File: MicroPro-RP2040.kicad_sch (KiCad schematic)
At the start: 55 parts, among them J1 USB_C_Receptacle_USB2.0_16P, J2 Qwiic, J3 Conn_02x12_Counter_Clockwise, J4 Conn_01x04, SW1 Boot, SW2 Reset, U1 RP2040, U2 AP2112K-3.3, U3 W25Q128JV, U5 TMUX1204DQAR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

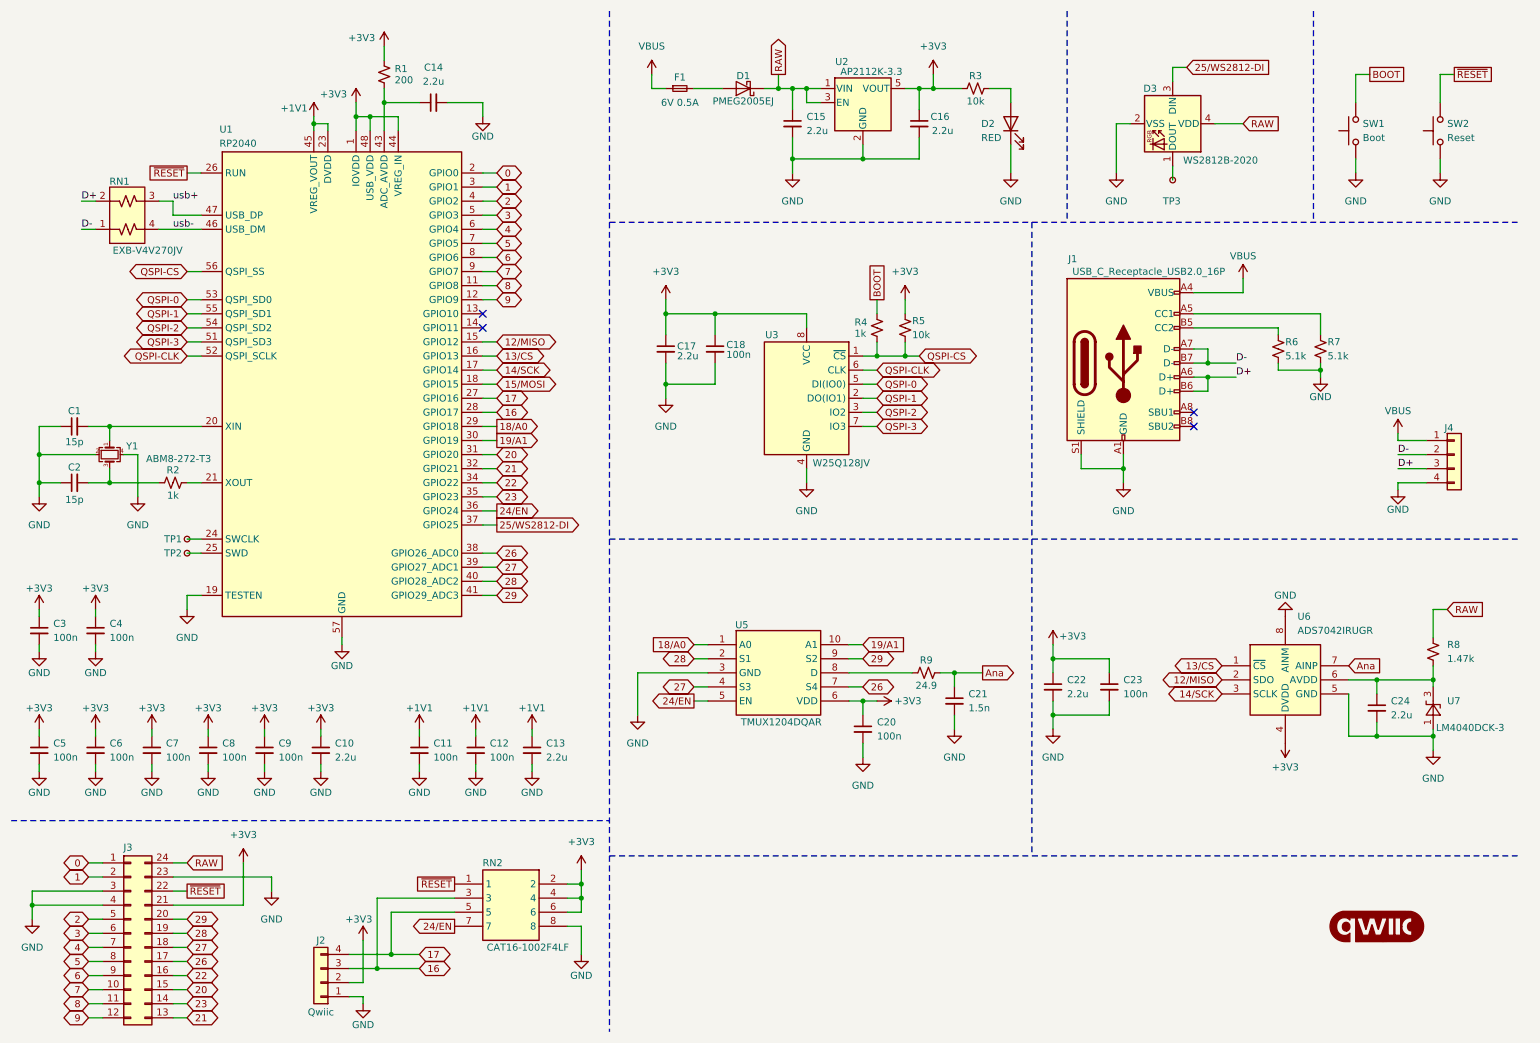
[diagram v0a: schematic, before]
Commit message: fixed miswiring in schematics, v1.1 board
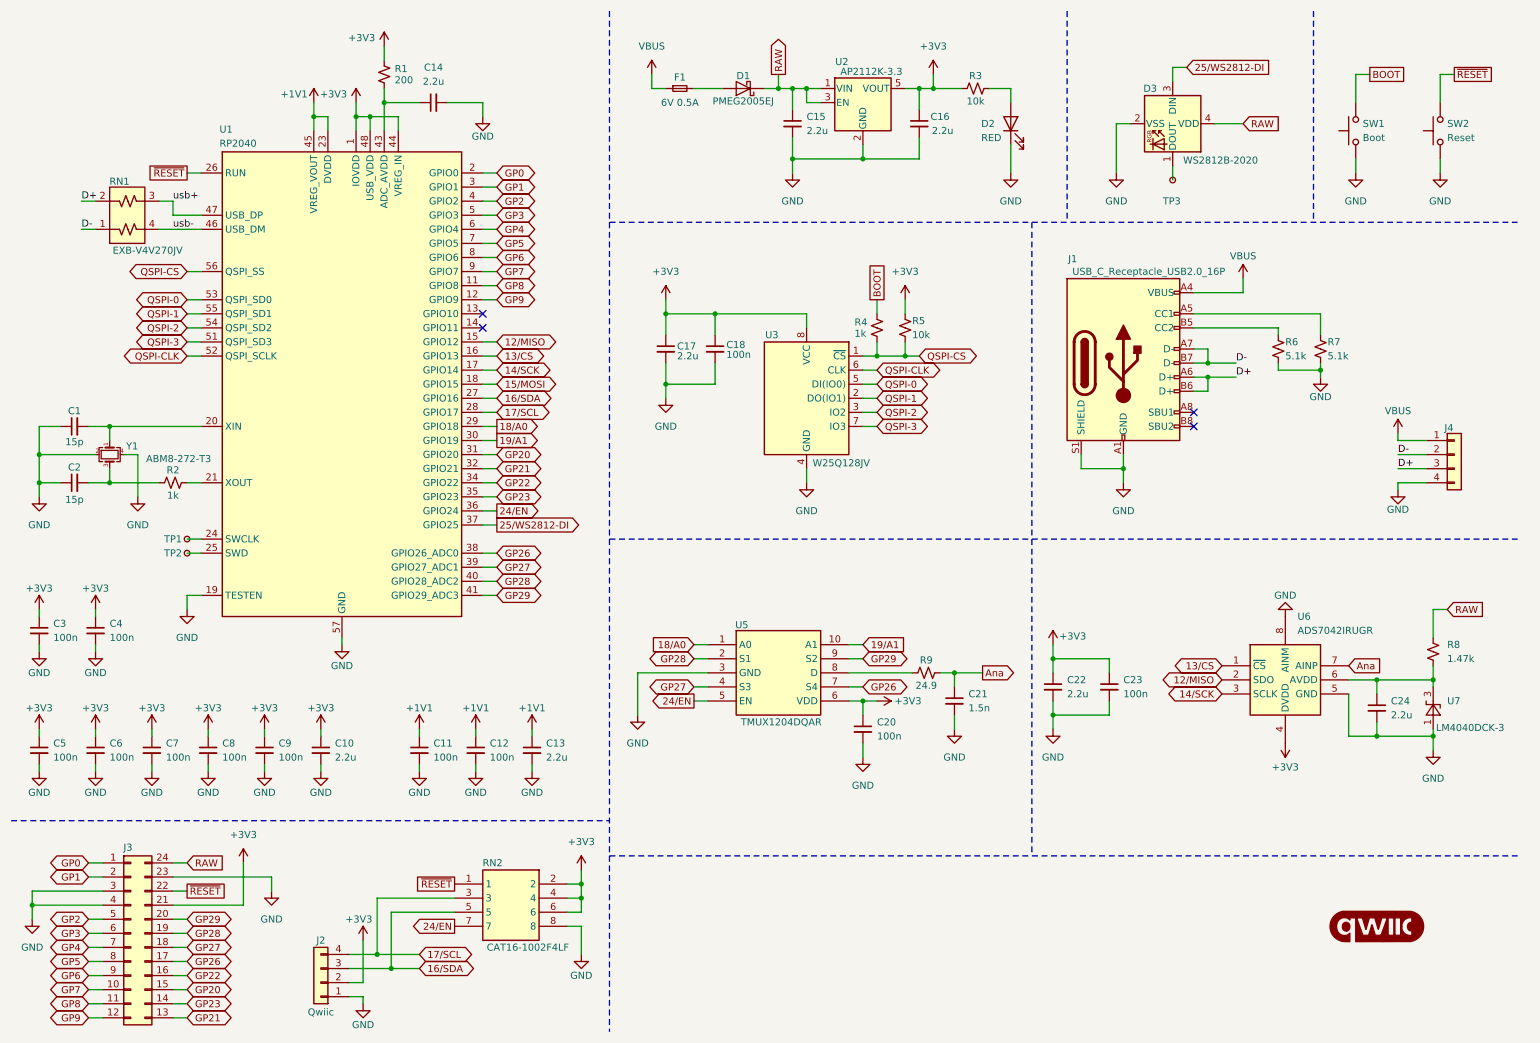
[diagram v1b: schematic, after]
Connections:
- net 0 renamed GP0
- net 1 renamed GP1
- net 16 renamed 17/SCL
- net 17/SCL: now also J2.4 (Pin_4); no longer J2.3 (Pin_3)
- net 17 renamed 16/SDA
- net 16/SDA: now also J2.3 (Pin_3); no longer J2.4 (Pin_4)
- net 2 renamed GP2
- net 20 renamed GP20
- net 21 renamed GP21
- net 22 renamed GP22
- net 23 renamed GP23
- net 26 renamed GP26
- net 27 renamed GP27
- net 28 renamed GP28
- net 29 renamed GP29
- net 3 renamed GP3
- net 4 renamed GP4
- net 5 renamed GP5
- net 6 renamed GP6
- net 7 renamed GP7
- net 8 renamed GP8
- net 9 renamed GP9

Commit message: generated gerber, added license, readme
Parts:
- R3: value 10k -> 5.1k
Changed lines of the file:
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@@
 	(title_block
 		(title "MicroPro RP2040")
-		(date "2024-10-05")
+		(date "2024-10-17")
 		(rev "v1.1")
 		(comment 3 "Author: Xiaotian Guan")
@@
 			)
 		)
-		(property "Value" "10k"
+		(property "Value" "5.1k"
 			(at 186.69 28.956 90)
 			(effects
